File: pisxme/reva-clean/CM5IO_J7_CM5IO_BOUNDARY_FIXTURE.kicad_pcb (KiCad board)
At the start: 6 copper layers, 188 x 110 mm, 7 parts, among them J2 A70-112-331N126, J7 Raspberry-Pi-5-Compute-Module, J7_BOUNDARY J7_LAUNCH_BOUNDARY, J9 THD-02-R, U6 TPD4EUSB30, U9 TPD4EUSB30

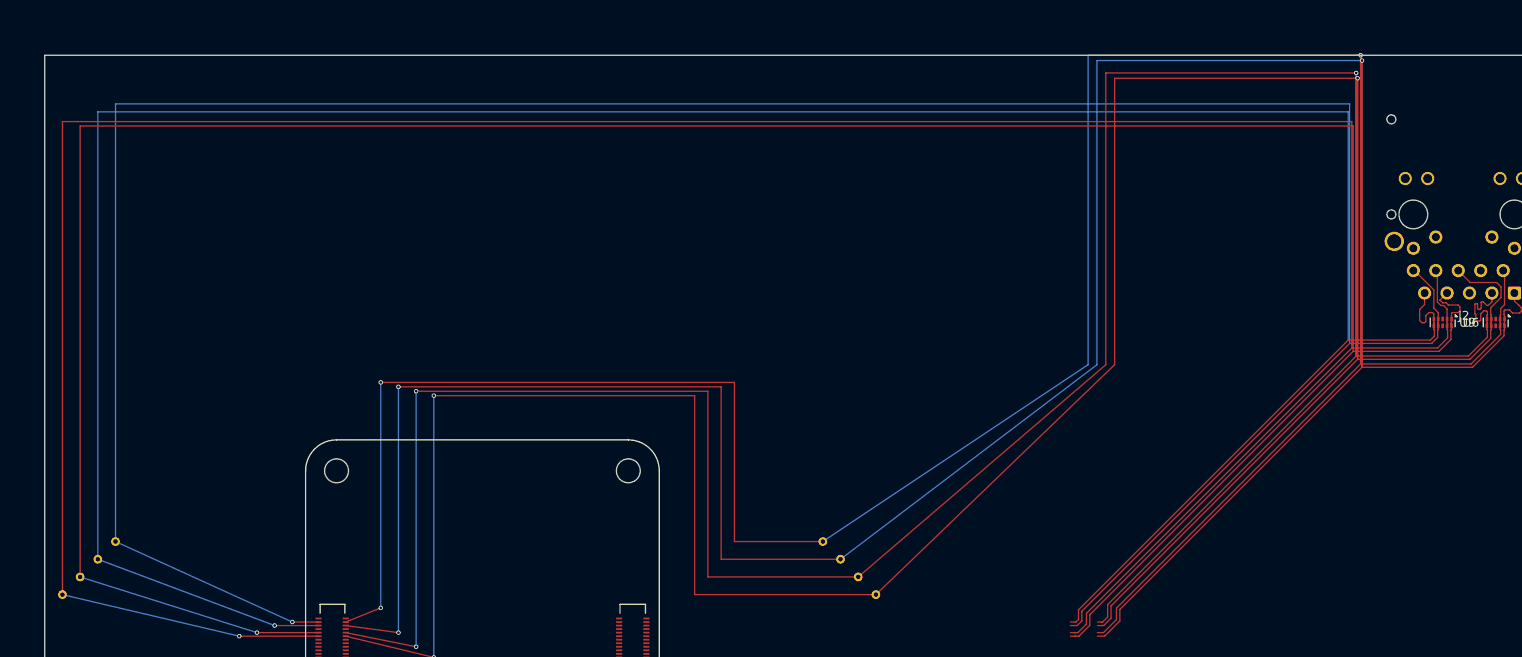
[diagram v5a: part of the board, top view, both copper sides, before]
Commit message: phase17: document real handoff transition limit
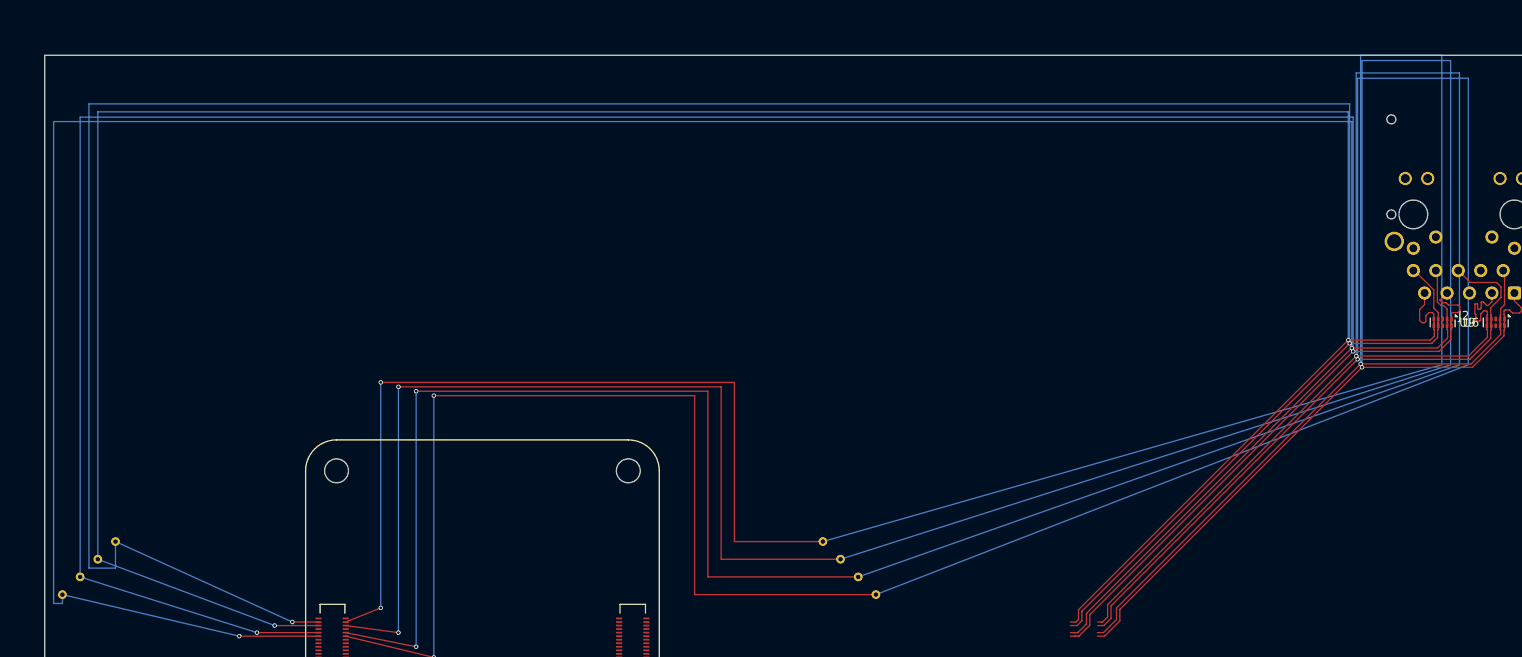
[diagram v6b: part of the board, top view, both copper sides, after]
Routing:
- net CM5_GBE_TD1_P: track 337.0 -> 317.2 mm, vias 3 -> 4
- net CM5_GBE_TD1_N: track 341.6 -> 323.0 mm, vias 3 -> 4
- net CM5_GBE_TD0_N: track 339.9 -> 326.5 mm, vias 3 -> 4
- net CM5_GBE_TD0_P: track 343.8 -> 331.5 mm, vias 3 -> 4
- net CM5_GBE_TD3_P: track 305.3 -> 317.3 mm, vias 1 -> 2
- net CM5_GBE_TD2_P: track 319.6 -> 323.6 mm, vias 1 -> 2
- net CM5_GBE_TD2_N: track 314.1 -> 316.1 mm, vias 1 -> 2
- net CM5_GBE_TD3_N: vias 1 -> 2

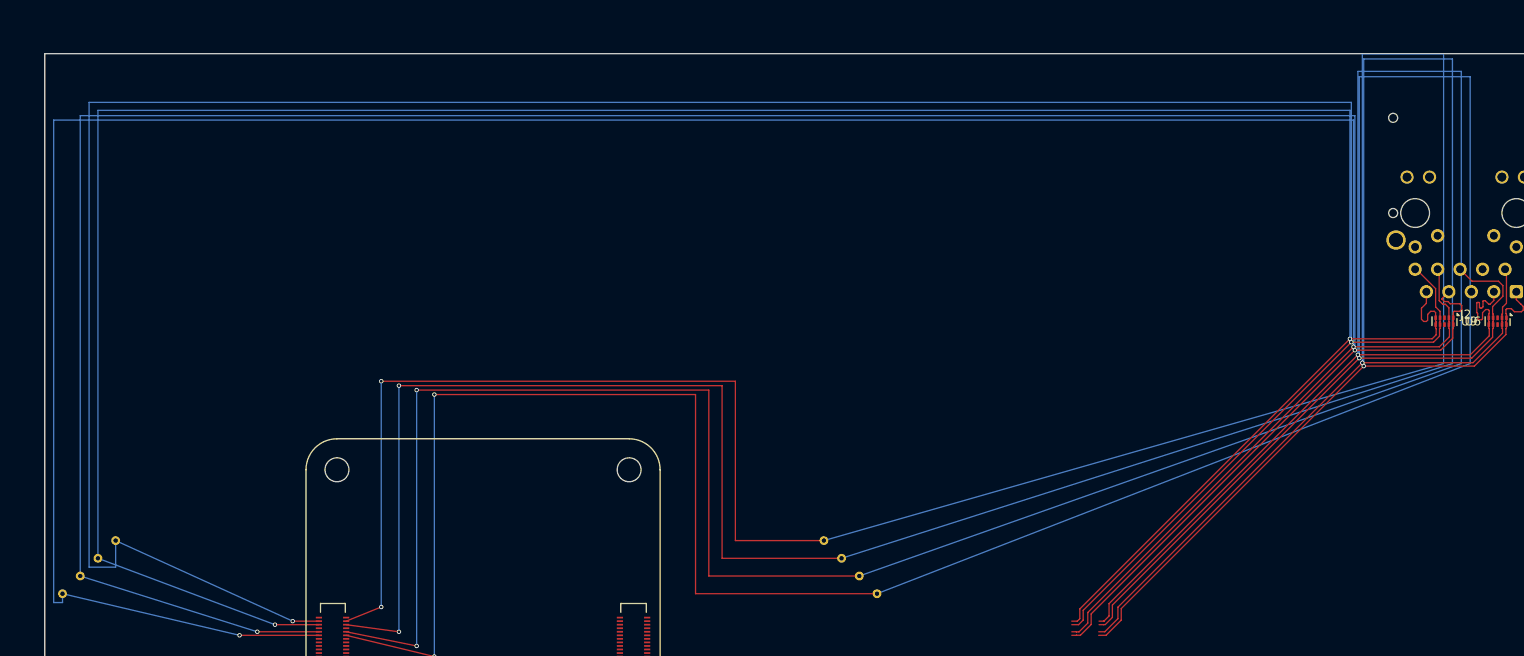
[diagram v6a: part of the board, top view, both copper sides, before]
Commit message: phase17: test separated ethernet fanout
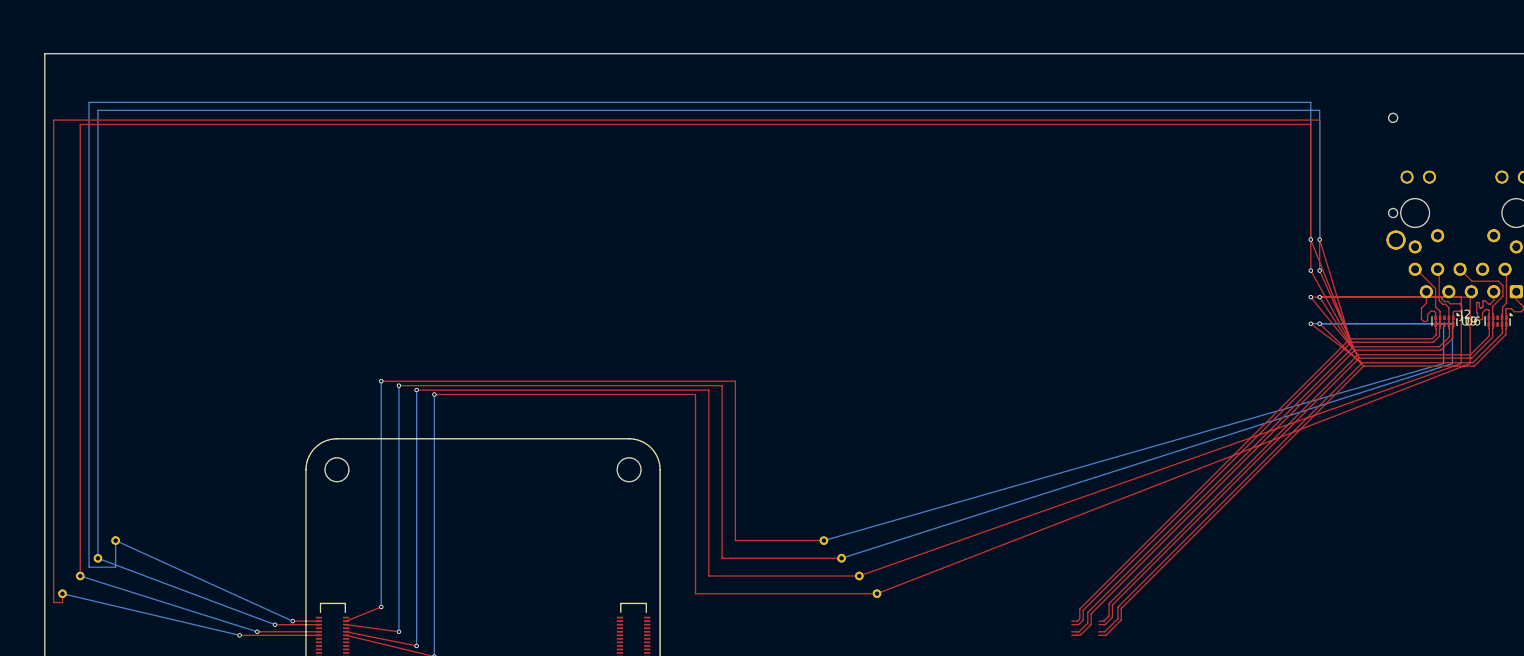
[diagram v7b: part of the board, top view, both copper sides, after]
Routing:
- net CM5_GBE_TD1_N: track 323.0 -> 270.3 mm
- net CM5_GBE_TD1_P: track 317.2 -> 264.9 mm
- net CM5_GBE_TD0_P: track 331.5 -> 287.5 mm, vias 4 -> 3
- net CM5_GBE_TD0_N: track 326.5 -> 282.7 mm, vias 4 -> 3
- net CM5_GBE_TD2_N: track 316.1 -> 310.4 mm, vias 2 -> 3
- net CM5_GBE_TD3_P: track 317.3 -> 313.6 mm
- net CM5_GBE_TD2_P: track 323.6 -> 320.5 mm, vias 2 -> 3
- net CM5_GBE_TD3_N: track 307.7 -> 304.8 mm
